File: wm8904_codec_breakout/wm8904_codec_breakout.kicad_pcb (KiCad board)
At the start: 2 copper layers, 40 x 40 mm, 30 parts, among them J101 Conn_01x12_Female, J102 Conn_01x12_Female, J103 AudioJack3, J104 AudioJack3, U101 AMS1117-1.8, U201 wm8904

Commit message: Order JLCPC V1
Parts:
- moved J103 5.65 mm to (144.0, 94.2), turned to 90 degrees
- moved J104 5.65 mm to (156.0, 94.2), turned to 90 degrees
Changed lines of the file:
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@@
   )
   (footprint "wm8904_breakout:PJ-320B-3A" (layer "F.Cu")
-    (at 156 99.9)
+    (at 156 94.25 90)
     (property "LCSC Part" "C707224")
     (property "Sheetfile" "wm8904_codec_breakout.kicad_sch")
     (property "Sheetname" "")
     (attr smd)
-    (fp_text reference "J104" (at 0.15 -12.3 unlocked) (layer "F.Fab")
-      (effects (font (size 1 1) (thickness 0.15)))
-    )
-    (fp_text value "AudioJack3" (at 0 4.1 unlocked) (layer "F.Fab")
-      (effects (font (size 1 1) (thickness 0.15)))
-    )
-    (fp_text user "${REFERENCE}" (at 0 6 unlocked) (layer "F.Fab")
-      (effects (font (size 1 1) (thickness 0.15)))
-    )
-    (fp_line (start -3 -1) (end -3 0) (layer "F.SilkS") (width 0.12))
-    (fp_line (start 3 -11.3) (end 3 -10.3) (layer "F.SilkS") (width 0.12))
-    (fp_line (start 2.5 1.7) (end 2.5 2.7) (layer "F.SilkS") (width 0.12))
-    (fp_line (start -2.5 1.7) (end -2.5 2.7) (layer "F.SilkS") (width 0.12))
-    (fp_line (start 3 0) (end 2 0) (layer "F.SilkS") (width 0.12))
-    (fp_line (start -3 0) (end -2 0) (layer "F.SilkS") (width 0.12))
-    (fp_line (start -3 -10.3) (end -3 -11.3) (layer "F.SilkS") (width 0.12))
-    (fp_line (start -2.5 2.7) (end -1.5 2.7) (layer "F.SilkS") (width 0.12))
-    (fp_line (start -3 -11.3) (end -2 -11.3) (layer "F.SilkS") (width 0.12))
-    (fp_line (start 2 -11.3) (end 3 -11.3) (layer "F.SilkS") (width 0.12))
-    (fp_line (start 3 -1) (end 3 0) (layer "F.SilkS") (width 0.12))
-    (fp_line (start 2.5 2.7) (end 1.5 2.7) (layer "F.SilkS") (width 0.12))
-    (fp_circle (center 0 -2.1) (end 0.6 -2.1) (layer "Edge.Cuts") (width 0.12) (fill none))
-    (fp_circle (center 0 -8.1) (end 0.6 -8.1) (layer "Edge.Cuts") (width 0.12) (fill none))
-    (fp_rect (start -5.6 -11.5) (end 5.6 2.9) (layer "F.CrtYd") (width 0.05) (fill none))
-    (fp_rect (start -2.5 0) (end 2.5 2.7) (layer "F.Fab") (width 0.1) (fill none))
-    (fp_rect (start -3 0) (end 3 -11.3) (layer "F.Fab") (width 0.1) (fill none))
-    (pad "R" smd rect (at -3.75 -4.1) (size 3.5 1.5) (layers "F.Cu" "F.Paste" "F.Mask")
+    (fp_text reference "J104" (at 0.15 -12.3 90 unlocked) (layer "F.Fab")
+      (effects (font (size 1 1) (thickness 0.15)))
+    )
+    (fp_text value "AudioJack3" (at 0 4.1 90 unlocked) (layer "F.Fab")
+      (effects (font (size 1 1) (thickness 0.15)))
+    )
+    (fp_text user "${REFERENCE}" (at 0 6 90 unlocked) (layer "F.Fab")
+      (effects (font (size 1 1) (thickness 0.15)))
+    )
+    (fp_line (start 5.65 3) (end 4.65 3) (layer "F.SilkS") (width 0.12))
+    (fp_line (start -7.35 2.5) (end -8.35 2.5) (layer "F.SilkS") (width 0.12))
+    (fp_line (start -5.65 3) (end -5.65 2) (layer "F.SilkS") (width 0.12))
+    (fp_line (start -4.65 -3) (end -5.65 -3) (layer "F.SilkS") (width 0.12))
+    (fp_line (start 5.65 2) (end 5.65 3) (layer "F.SilkS") (width 0.12))
+    (fp_line (start 5.65 -3) (end 5.65 -2) (layer "F.SilkS") (width 0.12))
+    (fp_line (start -8.35 2.5) (end -8.35 1.5) (layer "F.SilkS") (width 0.12))
+    (fp_line (start 4.65 -3) (end 5.65 -3) (layer "F.SilkS") (width 0.12))
+    (fp_line (start -5.65 -3) (end -5.65 -2) (layer "F.SilkS") (width 0.12))
+    (fp_line (start -7.35 -2.5) (end -8.35 -2.5) (layer "F.SilkS") (width 0.12))
+    (fp_line (start -8.35 -2.5) (end -8.35 -1.5) (layer "F.SilkS") (width 0.12))
+    (fp_line (start -4.65 3) (end -5.65 3) (layer "F.SilkS") (width 0.12))
+    (fp_circle (center -3.55 0) (end -3.55 0.6) (layer "Edge.Cuts") (width 0.12) (fill none))
+    (fp_circle (center 2.45 0) (end 2.45 0.6) (layer "Edge.Cuts") (width 0.12) (fill none))
+    (fp_rect (start 5.85 -5.6) (end -8.55 5.6) (layer "F.CrtYd") (width 0.05) (fill none))
+    (fp_rect (start -5.65 -3) (end 5.65 3) (layer "F.Fab") (width 0.1) (fill none))
+    (fp_rect (start -5.65 -2.5) (end -8.35 2.5) (layer "F.Fab") (width 0.1) (fill none))
+    (pad "R" smd rect (at -1.55 -3.75) (size 3.5 1.5) (layers "F.Cu" "F.Paste" "F.Mask")
       (net 13 "HPOUTR") (pintype "passive"))
-    (pad "S" smd rect (at 3.75 -2.1) (size 3.5 1.5) (layers "F.Cu" "F.Paste" "F.Mask")
-      (net 3 "GND") (pintype "passive"))
-    (pad "T" smd rect (at 3.75 -9.1) (size 3.5 1.5) (layers "F.Cu" "F.Paste" "F.Mask")
+    (pad "S" smd rect (at -3.55 3.75) (size 3.5 1.5) (layers "F.Cu" "F.Paste" "F.Mask")
+      (net 3 "GND") (pintype "passive"))
+    (pad "T" smd rect (at 3.45 3.75) (size 3.5 1.5) (layers "F.Cu" "F.Paste" "F.Mask")
       (net 12 "HPOUTL") (pintype "passive"))
   )
@@
   )
   (footprint "wm8904_breakout:PJ-320B-3A" (layer "F.Cu")
-    (at 144 99.9)
+    (at 144 94.25 90)
     (property "LCSC Part" "C707224")
     (property "Sheetfile" "wm8904_codec_breakout.kicad_sch")
     (property "Sheetname" "")
     (attr smd)
-    (fp_text reference "J103" (at 0.15 -12.3 unlocked) (layer "F.Fab")
-      (effects (font (size 1 1) (thickness 0.15)))
-    )
-    (fp_text value "AudioJack3" (at 0 4.1 unlocked) (layer "F.Fab")
-      (effects (font (size 1 1) (thickness 0.15)))
-    )
-    (fp_text user "${REFERENCE}" (at 0 6 unlocked) (layer "F.Fab")
-      (effects (font (size 1 1) (thickness 0.15)))
-    )
-    (fp_line (start -3 -11.3) (end -2 -11.3) (layer "F.SilkS") (width 0.12))
-    (fp_line (start 3 -11.3) (end 3 -10.3) (layer "F.SilkS") (width 0.12))
-    (fp_line (start -2.5 1.7) (end -2.5 2.7) (layer "F.SilkS") (width 0.12))
-    (fp_line (start -2.5 2.7) (end -1.5 2.7) (layer "F.SilkS") (width 0.12))
-    (fp_line (start -3 0) (end -2 0) (layer "F.SilkS") (width 0.12))
-    (fp_line (start 2.5 1.7) (end 2.5 2.7) (layer "F.SilkS") (width 0.12))
-    (fp_line (start 3 0) (end 2 0) (layer "F.SilkS") (width 0.12))
-    (fp_line (start 2 -11.3) (end 3 -11.3) (layer "F.SilkS") (width 0.12))
-    (fp_line (start -3 -1) (end -3 0) (layer "F.SilkS") (width 0.12))
-    (fp_line (start 3 -1) (end 3 0) (layer "F.SilkS") (width 0.12))
-    (fp_line (start -3 -10.3) (end -3 -11.3) (layer "F.SilkS") (width 0.12))
-    (fp_line (start 2.5 2.7) (end 1.5 2.7) (layer "F.SilkS") (width 0.12))
-    (fp_circle (center 0 -2.1) (end 0.6 -2.1) (layer "Edge.Cuts") (width 0.12) (fill none))
-    (fp_circle (center 0 -8.1) (end 0.6 -8.1) (layer "Edge.Cuts") (width 0.12) (fill none))
-    (fp_rect (start -5.6 -11.5) (end 5.6 2.9) (layer "F.CrtYd") (width 0.05) (fill none))
-    (fp_rect (start -2.5 0) (end 2.5 2.7) (layer "F.Fab") (width 0.1) (fill none))
-    (fp_rect (start -3 0) (end 3 -11.3) (layer "F.Fab") (width 0.1) (fill none))
-    (pad "R" smd rect (at -3.75 -4.1) (size 3.5 1.5) (layers "F.Cu" "F.Paste" "F.Mask")
+    (fp_text reference "J103" (at 0.15 -12.3 90 unlocked) (layer "F.Fab")
+      (effects (font (size 1 1) (thickness 0.15)))
+    )
+    (fp_text value "AudioJack3" (at 0 4.1 90 unlocked) (layer "F.Fab")
+      (effects (font (size 1 1) (thickness 0.15)))
+    )
+    (fp_text user "${REFERENCE}" (at 0 6 90 unlocked) (layer "F.Fab")
+      (effects (font (size 1 1) (thickness 0.15)))
+    )
+    (fp_line (start -8.35 -2.5) (end -8.35 -1.5) (layer "F.SilkS") (width 0.12))
+    (fp_line (start 5.65 -3) (end 5.65 -2) (layer "F.SilkS") (width 0.12))
+    (fp_line (start -4.65 3) (end -5.65 3) (layer "F.SilkS") (width 0.12))
+    (fp_line (start -5.65 3) (end -5.65 2) (layer "F.SilkS") (width 0.12))
+    (fp_line (start -5.65 -3) (end -5.65 -2) (layer "F.SilkS") (width 0.12))
+    (fp_line (start -7.35 2.5) (end -8.35 2.5) (layer "F.SilkS") (width 0.12))
+    (fp_line (start -8.35 2.5) (end -8.35 1.5) (layer "F.SilkS") (width 0.12))
+    (fp_line (start 5.65 3) (end 4.65 3) (layer "F.SilkS") (width 0.12))
+    (fp_line (start 4.65 -3) (end 5.65 -3) (layer "F.SilkS") (width 0.12))
+    (fp_line (start -7.35 -2.5) (end -8.35 -2.5) (layer "F.SilkS") (width 0.12))
+    (fp_line (start -4.65 -3) (end -5.65 -3) (layer "F.SilkS") (width 0.12))
+    (fp_line (start 5.65 2) (end 5.65 3) (layer "F.SilkS") (width 0.12))
+    (fp_circle (center 2.45 0) (end 2.45 0.6) (layer "Edge.Cuts") (width 0.12) (fill none))
+    (fp_circle (center -3.55 0) (end -3.55 0.6) (layer "Edge.Cuts") (width 0.12) (fill none))
+    (fp_rect (start 5.85 -5.6) (end -8.55 5.6) (layer "F.CrtYd") (width 0.05) (fill none))
+    (fp_rect (start -5.65 -3) (end 5.65 3) (layer "F.Fab") (width 0.1) (fill none))
+    (fp_rect (start -5.65 -2.5) (end -8.35 2.5) (layer "F.Fab") (width 0.1) (fill none))
+    (pad "R" smd rect (at -1.55 -3.75) (size 3.5 1.5) (layers "F.Cu" "F.Paste" "F.Mask")
       (net 16 "IN2R") (pintype "passive"))
-    (pad "S" smd rect (at 3.75 -2.1) (size 3.5 1.5) (layers "F.Cu" "F.Paste" "F.Mask")
-      (net 3 "GND") (pintype "passive"))
-    (pad "T" smd rect (at 3.75 -9.1) (size 3.5 1.5) (layers "F.Cu" "F.Paste" "F.Mask")
+    (pad "S" smd rect (at -3.55 3.75) (size 3.5 1.5) (layers "F.Cu" "F.Paste" "F.Mask")
+      (net 3 "GND") (pintype "passive"))
+    (pad "T" smd rect (at 3.45 3.75) (size 3.5 1.5) (layers "F.Cu" "F.Paste" "F.Mask")
       (net 14 "IN2L") (pintype "passive"))
   )

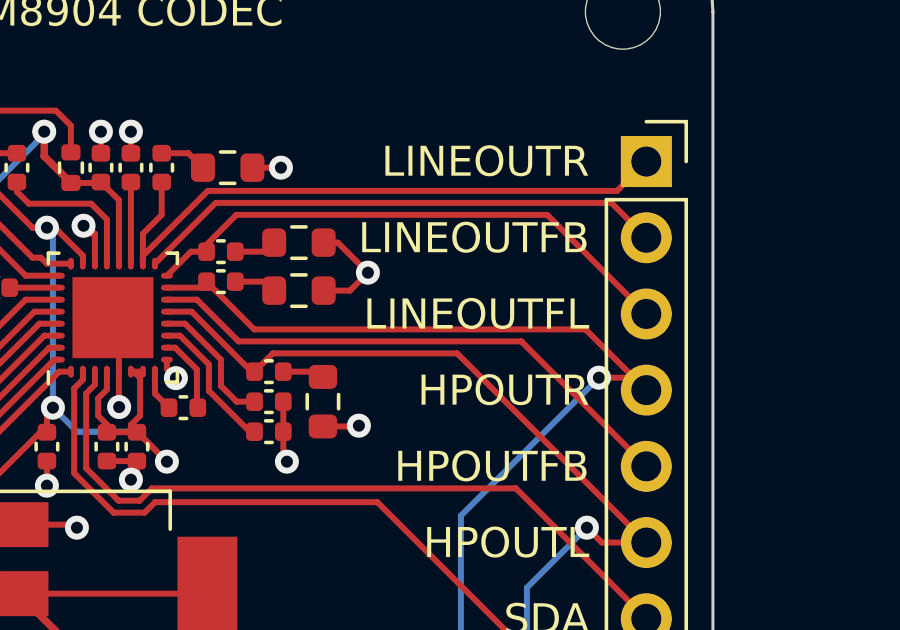
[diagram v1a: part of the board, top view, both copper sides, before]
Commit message: [wm8904_codec_breakout] Fix silkscreen typo (change LINEOUTFL to LINEOUTL)
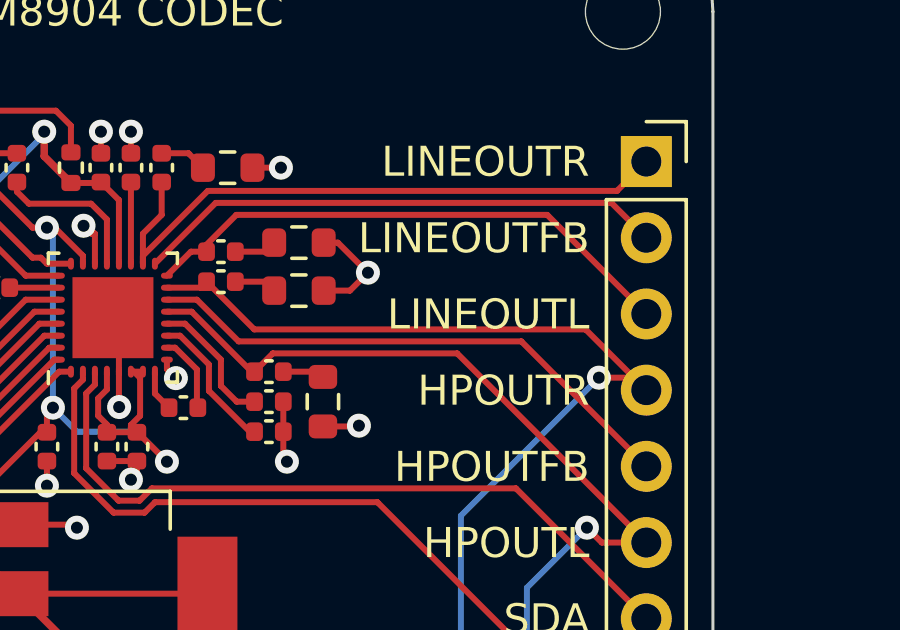
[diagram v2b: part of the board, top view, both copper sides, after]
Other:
- board text added: "LINEOUTL"
- board text removed: "LINEOUTFL"
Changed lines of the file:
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@@
     (effects (font (size 1 1) (thickness 0.15)) (justify right))
   )
-  (gr_text "LINEOUTFL" (at 165.886 73.096) (layer "F.SilkS")
+  (gr_text "LINEOUTL" (at 165.886 73.096) (layer "F.SilkS")
     (effects (font (size 1 1) (thickness 0.15)) (justify right))
   )
